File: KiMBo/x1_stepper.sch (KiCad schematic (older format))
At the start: 23 parts, among them U25 TMC2130

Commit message: More footprint association
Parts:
- R185, R186: footprint (none) -> Resistors_SMD:R_0805
- U25: footprint (none) -> KiMBo:QFN36_5X6
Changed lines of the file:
@@
 $EndComp
 $Comp
-L GND #PWR0250
+L GND #PWR0251
 U 1 1 5BA7E13F
 P 7500 3300
-F 0 "#PWR0250" H 7500 3050 50  0001 C CNN
+F 0 "#PWR0251" H 7500 3050 50  0001 C CNN
 F 1 "GND" H 7500 3150 50  0000 C CNN
 F 2 "" H 7500 3300 50  0000 C CNN
@@
 $EndComp
 $Comp
-L GND #PWR0251
+L GND #PWR0252
 U 1 1 58C092DF
 P 10350 3350
-F 0 "#PWR0251" H 10350 3100 50  0001 C CNN
+F 0 "#PWR0252" H 10350 3100 50  0001 C CNN
 F 1 "GND" H 10355 3177 50  0000 C CNN
 F 2 "" H 10350 3350 50  0000 C CNN
@@
 $EndComp
 $Comp
-L +24V #PWR0252
+L +24V #PWR0253
 U 1 1 5BA7E142
 P 8550 2850
-F 0 "#PWR0252" H 8550 2700 50  0001 C CNN
+F 0 "#PWR0253" H 8550 2700 50  0001 C CNN
 F 1 "+24V" H 8565 3023 50  0000 C CNN
 F 2 "" H 8550 2850 50  0000 C CNN
@@
 F 0 "R186" H 10700 6650 50  0000 R CNN
 F 1 "220mΩ" H 10700 6750 50  0000 R CNN
-F 2 "" V 10680 6700 50  0001 C CNN
+F 2 "Resistors_SMD:R_0805" V 10680 6700 50  0001 C CNN
 F 3 "" H 10750 6700 50  0000 C CNN
 	1    10750 6700
@@
 F 0 "R185" H 9900 6650 50  0000 R CNN
 F 1 "220mΩ" H 9900 6750 50  0000 R CNN
-F 2 "" V 9880 6700 50  0001 C CNN
+F 2 "Resistors_SMD:R_0805" V 9880 6700 50  0001 C CNN
 F 3 "" H 9950 6700 50  0000 C CNN
 	1    9950 6700
@@
 $EndComp
 $Comp
-L GND #PWR0253
+L GND #PWR0254
 U 1 1 58C09300
 P 9650 7050
-F 0 "#PWR0253" H 9650 6800 50  0001 C CNN
+F 0 "#PWR0254" H 9650 6800 50  0001 C CNN
 F 1 "GND" H 9655 6877 50  0000 C CNN
 F 2 "" H 9650 7050 50  0000 C CNN
@@
 NoConn ~ 7700 5700
 $Comp
-L GND #PWR0254
+L GND #PWR0255
 U 1 1 58C09323
 P 7650 6100
-F 0 "#PWR0254" H 7650 5850 50  0001 C CNN
+F 0 "#PWR0255" H 7650 5850 50  0001 C CNN
 F 1 "GND" H 7655 5927 50  0000 C CNN
 F 2 "" H 7650 6100 50  0000 C CNN
@@
 $EndComp
 $Comp
-L GND #PWR0255
+L GND #PWR0256
 U 1 1 5BA7E152
 P 9250 5200
-F 0 "#PWR0255" H 9250 4950 50  0001 C CNN
+F 0 "#PWR0256" H 9250 4950 50  0001 C CNN
 F 1 "GND" H 9250 5050 50  0000 C CNN
 F 2 "" H 9250 5200 50  0000 C CNN
@@
 $EndComp
 $Comp
-L GND #PWR0256
+L GND #PWR0257
 U 1 1 5BA7E155
 P 9250 6050
-F 0 "#PWR0256" H 9250 5800 50  0001 C CNN
+F 0 "#PWR0257" H 9250 5800 50  0001 C CNN
 F 1 "GND" H 9250 5900 50  0000 C CNN
 F 2 "" H 9250 6050 50  0000 C CNN
@@
 F 0 "U25" H 7950 6200 60  0000 C CNN
 F 1 "TMC2130" H 8700 6200 60  0000 C CNN
-F 2 "" H 8400 5000 60  0001 C CNN
+F 2 "KiMBo:QFN36_5X6" H 8400 5000 60  0001 C CNN
 F 3 "" H 8400 5000 60  0000 C CNN
 	1    8400 4700
@@
 	6400 3500 7700 3500
 $Comp
-L VDD_3V3B #PWR0257
+L VDD_3V3B #PWR0258
 U 1 1 5BA7E15A
 P 6750 3450
-F 0 "#PWR0257" H 6750 3300 50  0001 C CNN
+F 0 "#PWR0258" H 6750 3300 50  0001 C CNN
 F 1 "VDD_3V3B" H 6765 3623 50  0000 C CNN
 F 2 "" H 6750 3450 50  0000 C CNN

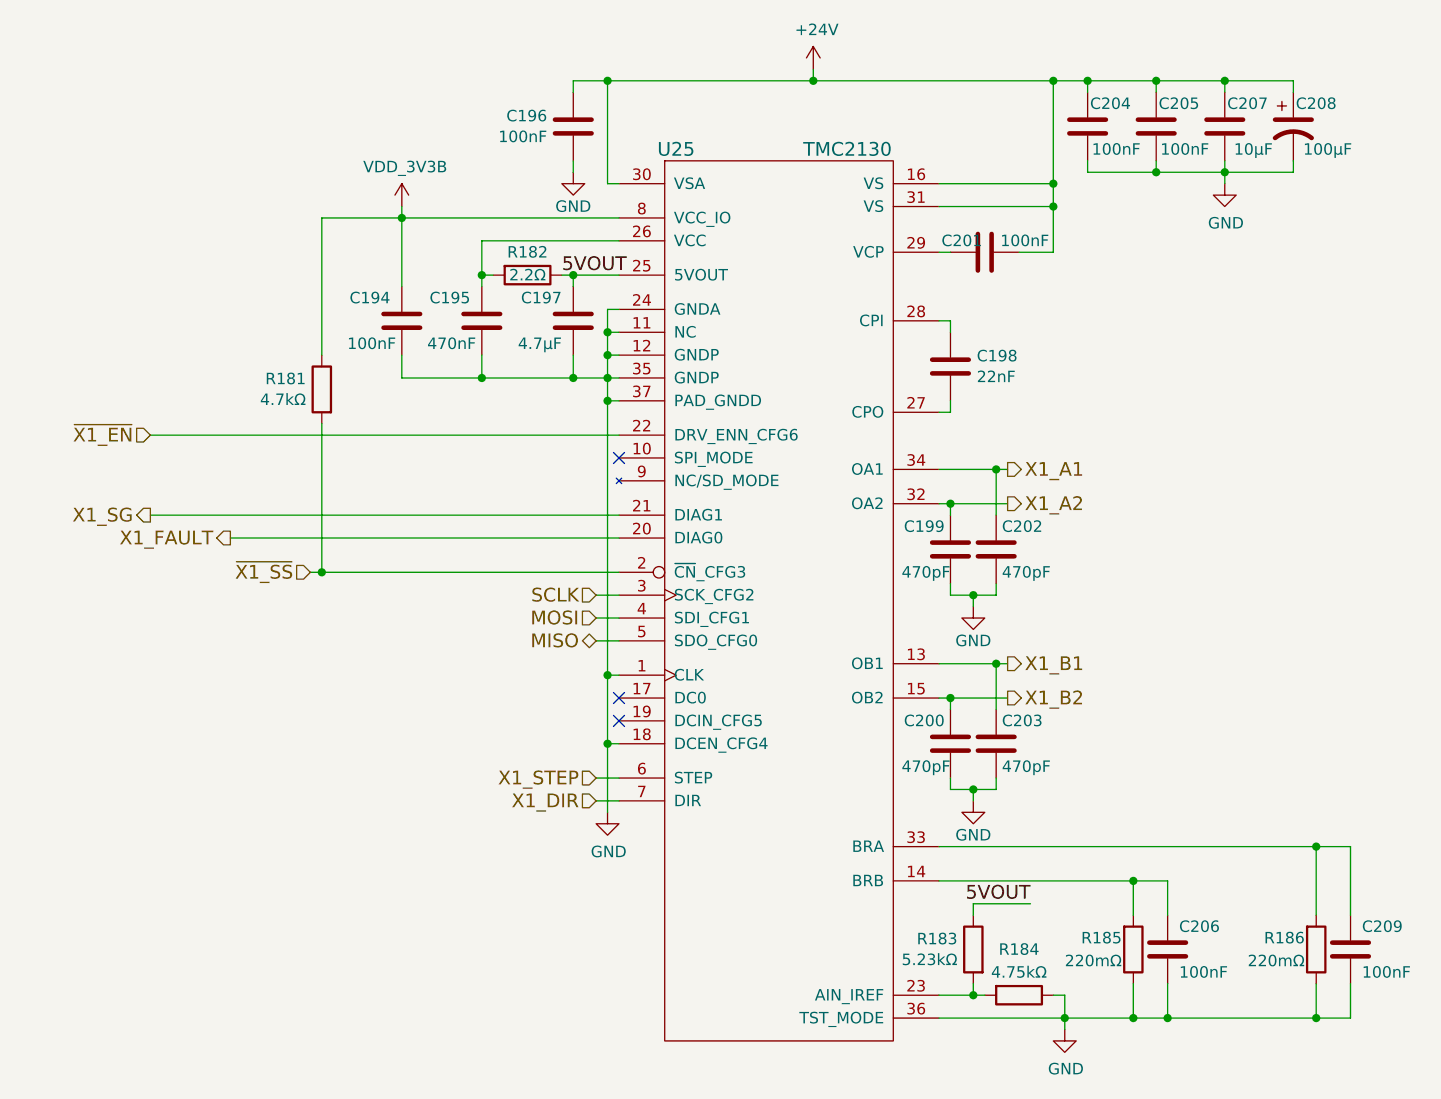
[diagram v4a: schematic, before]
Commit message: Add more footprints and more associations, one association left!
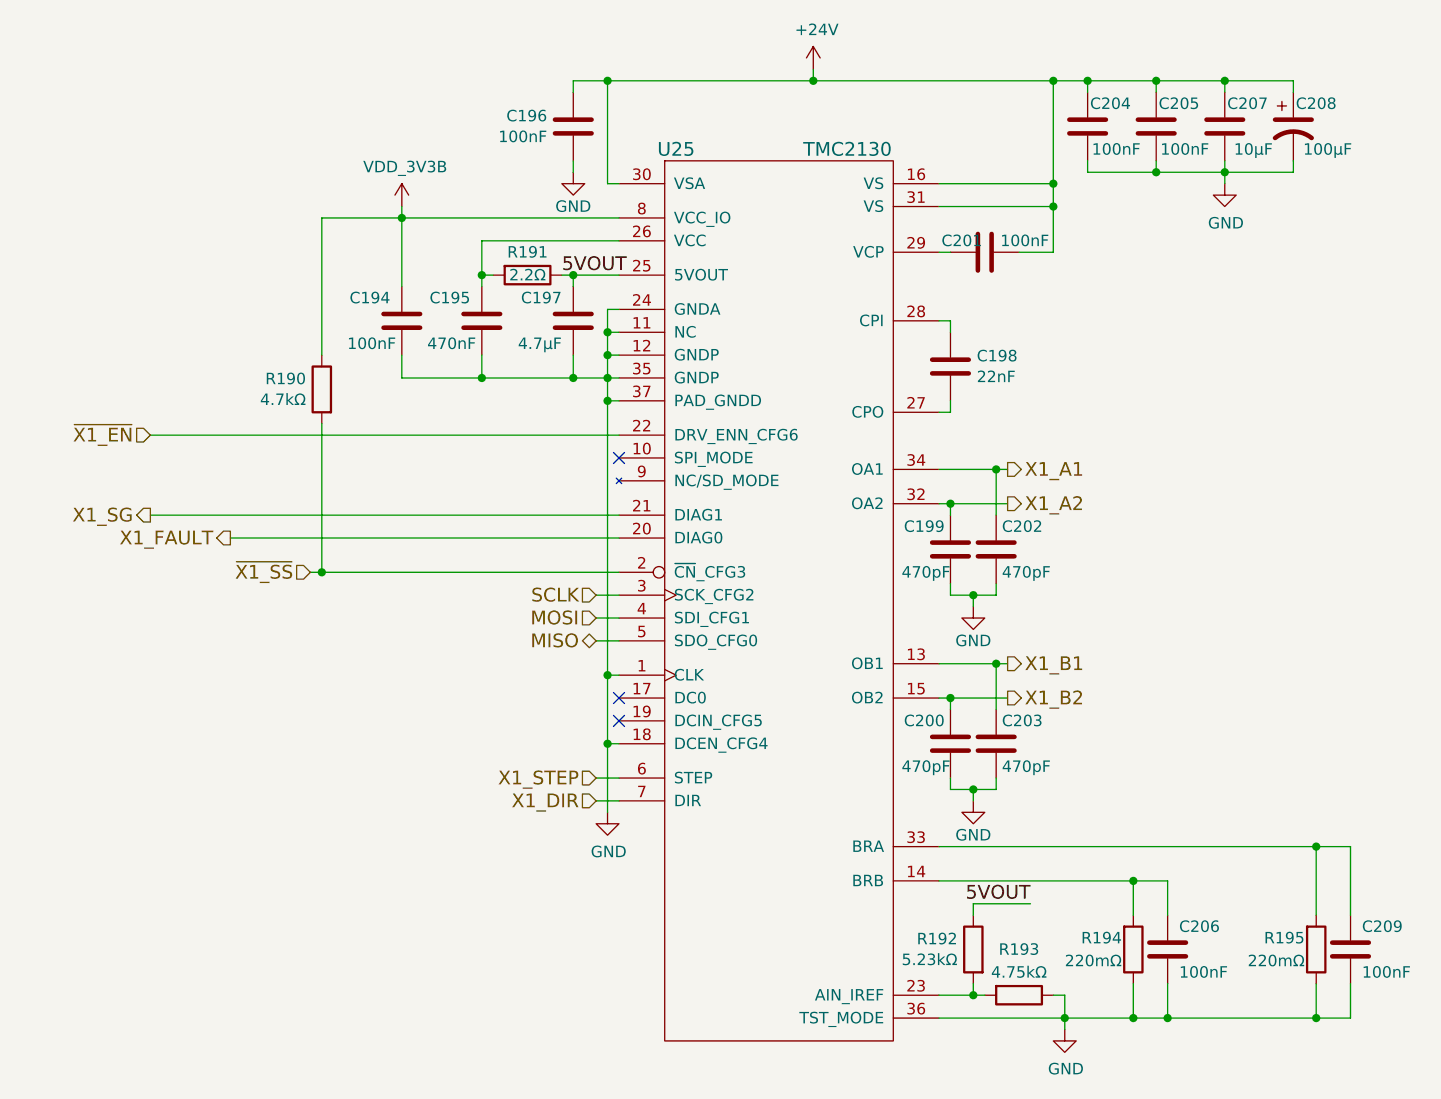
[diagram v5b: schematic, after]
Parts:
- R193: renamed from R184; footprint Resistors_SMD:R_0603 -> Resistors_SMD:R_0805
- R195: renamed from R186; footprint Resistors_SMD:R_0805 -> Resistors_SMD:R_0603
- renumbered R181 to R190, R182 to R191, R183 to R192, R185 to R194
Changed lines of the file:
@@
 $EndComp
 $Comp
-L GND #PWR0251
+L GND #PWR0253
 U 1 1 5BA7E13F
 P 7500 3300
-F 0 "#PWR0251" H 7500 3050 50  0001 C CNN
+F 0 "#PWR0253" H 7500 3050 50  0001 C CNN
 F 1 "GND" H 7500 3150 50  0000 C CNN
 F 2 "" H 7500 3300 50  0000 C CNN
@@
 $EndComp
 $Comp
-L GND #PWR0252
+L GND #PWR0254
 U 1 1 58C092DF
 P 10350 3350
-F 0 "#PWR0252" H 10350 3100 50  0001 C CNN
+F 0 "#PWR0254" H 10350 3100 50  0001 C CNN
 F 1 "GND" H 10355 3177 50  0000 C CNN
 F 2 "" H 10350 3350 50  0000 C CNN
@@
 $EndComp
 $Comp
-L +24V #PWR0253
+L +24V #PWR0255
 U 1 1 5BA7E142
 P 8550 2850
-F 0 "#PWR0253" H 8550 2700 50  0001 C CNN
+F 0 "#PWR0255" H 8550 2700 50  0001 C CNN
 F 1 "+24V" H 8565 3023 50  0000 C CNN
 F 2 "" H 8550 2850 50  0000 C CNN
@@
 $EndComp
 $Comp
-L R R186
+L R R195
 U 1 1 5BA7E144
 P 10750 6700
-F 0 "R186" H 10700 6650 50  0000 R CNN
+F 0 "R195" H 10700 6650 50  0000 R CNN
 F 1 "220mΩ" H 10700 6750 50  0000 R CNN
-F 2 "Resistors_SMD:R_0805" V 10680 6700 50  0001 C CNN
+F 2 "Resistors_SMD:R_0603" V 10680 6700 50  0001 C CNN
 F 3 "" H 10750 6700 50  0000 C CNN
 	1    10750 6700
@@
 $EndComp
 $Comp
-L R R185
+L R R194
 U 1 1 5BA7E145
 P 9950 6700
-F 0 "R185" H 9900 6650 50  0000 R CNN
+F 0 "R194" H 9900 6650 50  0000 R CNN
 F 1 "220mΩ" H 9900 6750 50  0000 R CNN
 F 2 "Resistors_SMD:R_0805" V 9880 6700 50  0001 C CNN
@@
 $EndComp
 $Comp
-L GND #PWR0254
+L GND #PWR0256
 U 1 1 58C09300
 P 9650 7050
-F 0 "#PWR0254" H 9650 6800 50  0001 C CNN
+F 0 "#PWR0256" H 9650 6800 50  0001 C CNN
 F 1 "GND" H 9655 6877 50  0000 C CNN
 F 2 "" H 9650 7050 50  0000 C CNN
@@
 NoConn ~ 7700 5600
 $Comp
-L R R182
+L R R191
 U 1 1 58C09307
 P 7300 3750
-F 0 "R182" V 7200 3750 50  0000 C CNN
+F 0 "R191" V 7200 3750 50  0000 C CNN
 F 1 "2.2Ω" V 7300 3750 50  0000 C CNN
 F 2 "Resistors_SMD:R_0603" V 7230 3750 50  0001 C CNN
@@
 NoConn ~ 7700 5700
 $Comp
-L GND #PWR0255
+L GND #PWR0257
 U 1 1 58C09323
 P 7650 6100
-F 0 "#PWR0255" H 7650 5850 50  0001 C CNN
+F 0 "#PWR0257" H 7650 5850 50  0001 C CNN
 F 1 "GND" H 7655 5927 50  0000 C CNN
 F 2 "" H 7650 6100 50  0000 C CNN
@@
 5VOUT
 $Comp
-L R R183
+L R R192
 U 1 1 58C09343
 P 9250 6700
-F 0 "R183" H 9319 6746 50  0000 L CNN
+F 0 "R192" H 9319 6746 50  0000 L CNN
 F 1 "5.23kΩ" H 9319 6655 50  0000 L CNN
 F 2 "Resistors_SMD:R_0603" V 9180 6700 50  0001 C CNN
@@
 5VOUT
 $Comp
-L R R184
+L R R193
 U 1 1 58C0934B
 P 9450 6900
-F 0 "R184" V 9250 6900 50  0000 C CNN
+F 0 "R193" V 9250 6900 50  0000 C CNN
 F 1 "4.75kΩ" V 9350 6900 50  0000 C CNN
-F 2 "Resistors_SMD:R_0603" V 9380 6900 50  0001 C CNN
+F 2 "Resistors_SMD:R_0805" V 9380 6900 50  0001 C CNN
 F 3 "" H 9450 6900 50  0000 C CNN
 	1    9450 6900
@@
 $EndComp
 $Comp
-L R R181
+L R R190
 U 1 1 5BA7E14F
 P 6400 4250
-F 0 "R181" H 6469 4296 50  0000 L CNN
+F 0 "R190" H 6469 4296 50  0000 L CNN
 F 1 "4.7kΩ" H 6469 4205 50  0000 L CNN
 F 2 "Resistors_SMD:R_0603" V 6330 4250 50  0001 C CNN
@@
 $EndComp
 $Comp
-L GND #PWR0256
+L GND #PWR0258
 U 1 1 5BA7E152
 P 9250 5200
-F 0 "#PWR0256" H 9250 4950 50  0001 C CNN
+F 0 "#PWR0258" H 9250 4950 50  0001 C CNN
 F 1 "GND" H 9250 5050 50  0000 C CNN
 F 2 "" H 9250 5200 50  0000 C CNN
@@
 $EndComp
 $Comp
-L GND #PWR0257
+L GND #PWR0259
 U 1 1 5BA7E155
 P 9250 6050
-F 0 "#PWR0257" H 9250 5800 50  0001 C CNN
+F 0 "#PWR0259" H 9250 5800 50  0001 C CNN
 F 1 "GND" H 9250 5900 50  0000 C CNN
 F 2 "" H 9250 6050 50  0000 C CNN
@@
 	6400 3500 7700 3500
 $Comp
-L VDD_3V3B #PWR0258
+L VDD_3V3B #PWR0260
 U 1 1 5BA7E15A
 P 6750 3450
-F 0 "#PWR0258" H 6750 3300 50  0001 C CNN
+F 0 "#PWR0260" H 6750 3300 50  0001 C CNN
 F 1 "VDD_3V3B" H 6765 3623 50  0000 C CNN
 F 2 "" H 6750 3450 50  0000 C CNN

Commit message: Begin layout
Arrange all connectors to get a feel for the area.
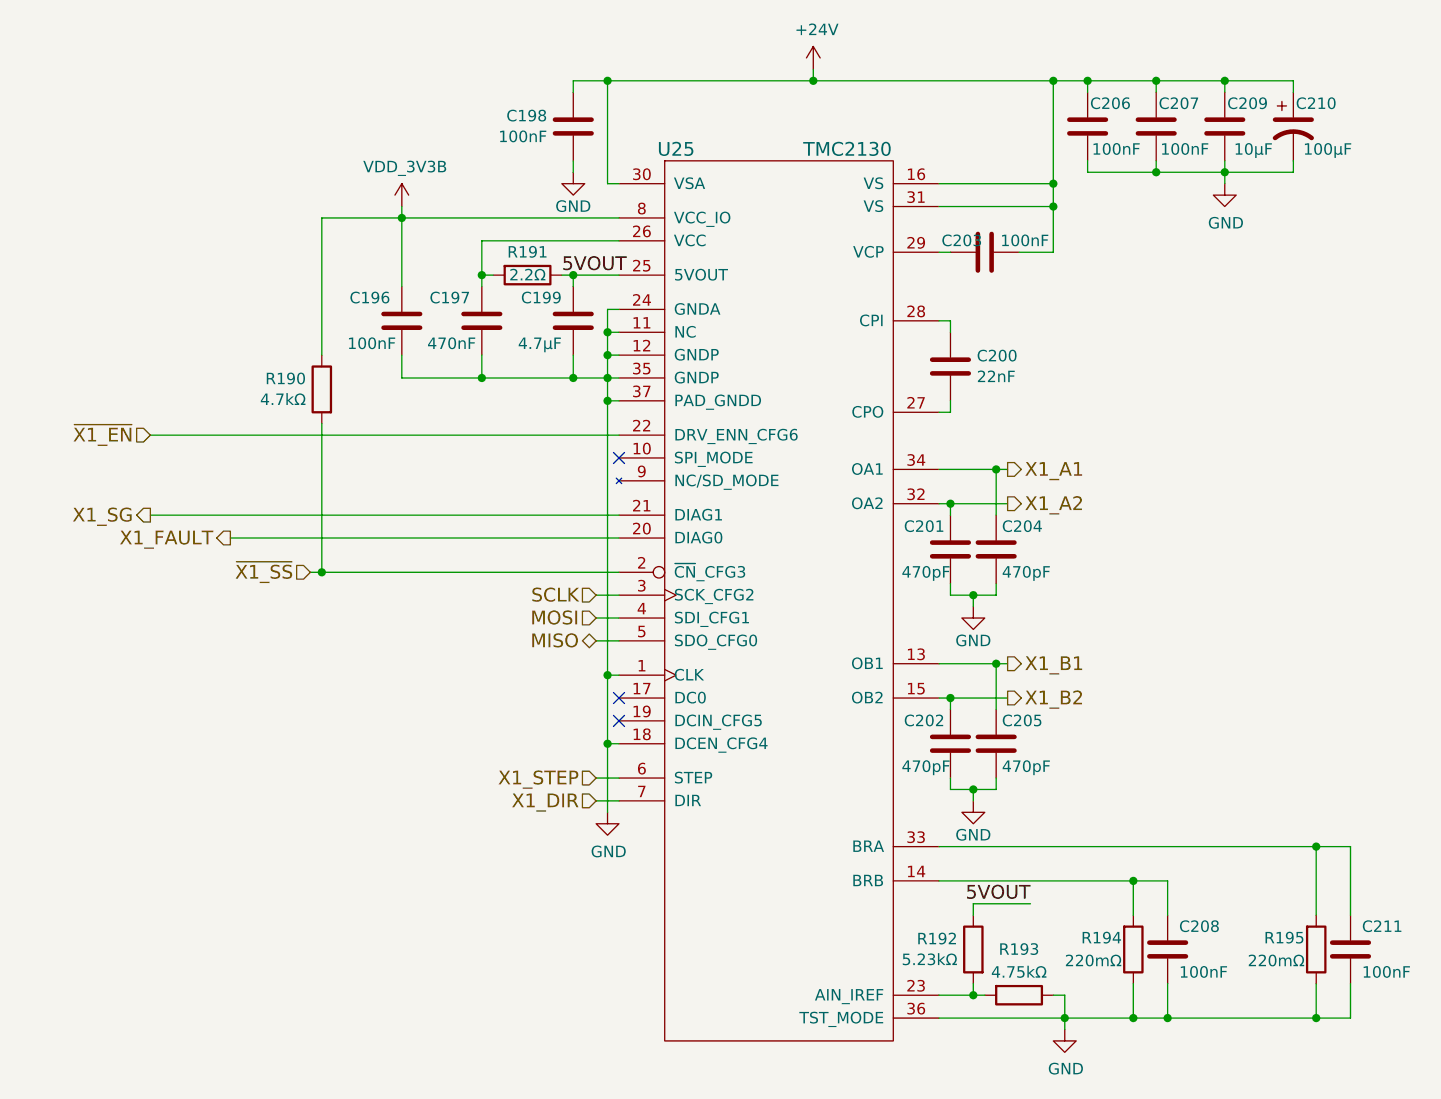
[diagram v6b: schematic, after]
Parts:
- renumbered C194 to C196, C195 to C197, C196 to C198, C197 to C199, C198 to C200, C199 to C201, C200 to C202, C201 to C203, C202 to C204, C203 to C205, C204 to C206, C205 to C207, C206 to C208, C207 to C209, C208 to C210, C209 to C211
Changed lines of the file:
@@
 X1_SG
 $Comp
-L C C196
+L C C198
 U 1 1 58C092B6
 P 7500 3100
-F 0 "C196" H 7386 3054 50  0000 R CNN
+F 0 "C198" H 7386 3054 50  0000 R CNN
 F 1 "100nF" H 7386 3145 50  0000 R CNN
 F 2 "Capacitors_SMD:C_0603" H 7538 2950 50  0001 C CNN
@@
 $EndComp
 $Comp
-L C C201
+L C C203
 U 1 1 58C092BD
 P 9300 3650
-F 0 "C201" V 9250 3550 50  0000 C CNN
+F 0 "C203" V 9250 3550 50  0000 C CNN
 F 1 "100nF" V 9250 3825 50  0000 C CNN
 F 2 "Capacitors_SMD:C_0603" H 9338 3500 50  0001 C CNN
@@
 $EndComp
 $Comp
-L CP1 C208
+L CP1 C210
 U 1 1 5BA7E13D
 P 10650 3100
-F 0 "C208" H 10750 3200 50  0000 C CNN
+F 0 "C210" H 10750 3200 50  0000 C CNN
 F 1 "100μF" H 10800 3000 50  0000 C CNN
 F 2 "Capacitors_SMD:c_elec_8x10" H 10650 3100 50  0001 C CNN
@@
 $EndComp
 $Comp
-L C C204
+L C C206
 U 1 1 5BA7E13E
 P 9750 3100
-F 0 "C204" H 9650 3200 50  0000 C CNN
+F 0 "C206" H 9650 3200 50  0000 C CNN
 F 1 "100nF" H 9625 3000 50  0000 C CNN
 F 2 "Capacitors_SMD:C_0603" H 9788 2950 50  0001 C CNN
@@
 $EndComp
 $Comp
-L GND #PWR0253
+L GND #PWR0256
 U 1 1 5BA7E13F
 P 7500 3300
-F 0 "#PWR0253" H 7500 3050 50  0001 C CNN
+F 0 "#PWR0256" H 7500 3050 50  0001 C CNN
 F 1 "GND" H 7500 3150 50  0000 C CNN
 F 2 "" H 7500 3300 50  0000 C CNN
@@
 $EndComp
 $Comp
-L C C205
+L C C207
 U 1 1 58C092D8
 P 10050 3100
-F 0 "C205" H 9950 3200 50  0000 C CNN
+F 0 "C207" H 9950 3200 50  0000 C CNN
 F 1 "100nF" H 9925 3000 50  0000 C CNN
 F 2 "Capacitors_SMD:C_0603" H 10088 2950 50  0001 C CNN
@@
 $EndComp
 $Comp
-L GND #PWR0254
+L GND #PWR0257
 U 1 1 58C092DF
 P 10350 3350
-F 0 "#PWR0254" H 10350 3100 50  0001 C CNN
+F 0 "#PWR0257" H 10350 3100 50  0001 C CNN
 F 1 "GND" H 10355 3177 50  0000 C CNN
 F 2 "" H 10350 3350 50  0000 C CNN
@@
 $EndComp
 $Comp
-L +24V #PWR0255
+L +24V #PWR0258
 U 1 1 5BA7E142
 P 8550 2850
-F 0 "#PWR0255" H 8550 2700 50  0001 C CNN
+F 0 "#PWR0258" H 8550 2700 50  0001 C CNN
 F 1 "+24V" H 8565 3023 50  0000 C CNN
 F 2 "" H 8550 2850 50  0000 C CNN
@@
 $EndComp
 $Comp
-L C C198
+L C C200
 U 1 1 5BA7E143
 P 9150 4150
-F 0 "C198" H 9265 4196 50  0000 L CNN
+F 0 "C200" H 9265 4196 50  0000 L CNN
 F 1 "22nF" H 9265 4105 50  0000 L CNN
 F 2 "Capacitors_SMD:C_0603" H 9188 4000 50  0001 C CNN
@@
 $EndComp
 $Comp
-L GND #PWR0256
+L GND #PWR0259
 U 1 1 58C09300
 P 9650 7050
-F 0 "#PWR0256" H 9650 6800 50  0001 C CNN
+F 0 "#PWR0259" H 9650 6800 50  0001 C CNN
 F 1 "GND" H 9655 6877 50  0000 C CNN
 F 2 "" H 9650 7050 50  0000 C CNN
@@
 $EndComp
 $Comp
-L C C195
+L C C197
 U 1 1 58C0930E
 P 7100 3950
-F 0 "C195" H 7150 4050 50  0000 L CNN
+F 0 "C197" H 7150 4050 50  0000 L CNN
 F 1 "470nF" H 7125 3850 50  0000 L CNN
 F 2 "Capacitors_SMD:C_0603" H 7138 3800 50  0001 C CNN
@@
 NoConn ~ 7700 5700
 $Comp
-L GND #PWR0257
+L GND #PWR0260
 U 1 1 58C09323
 P 7650 6100
-F 0 "#PWR0257" H 7650 5850 50  0001 C CNN
+F 0 "#PWR0260" H 7650 5850 50  0001 C CNN
 F 1 "GND" H 7655 5927 50  0000 C CNN
 F 2 "" H 7650 6100 50  0000 C CNN
@@
 $EndComp
 $Comp
-L C C206
+L C C208
 U 1 1 58C09329
 P 10100 6700
-F 0 "C206" H 10150 6800 50  0000 L CNN
+F 0 "C208" H 10150 6800 50  0000 L CNN
 F 1 "100nF" H 10150 6600 50  0000 L CNN
 F 2 "Capacitors_SMD:C_0603" H 10138 6550 50  0001 C CNN
@@
 NoConn ~ 7700 4550
 $Comp
-L C C197
+L C C199
 U 1 1 58C0933B
 P 7500 3950
-F 0 "C197" H 7550 4050 50  0000 L CNN
+F 0 "C199" H 7550 4050 50  0000 L CNN
 F 1 "4.7μF" H 7550 3850 50  0000 L CNN
 F 2 "Capacitors_SMD:C_0603" H 7538 3800 50  0001 C CNN
@@
 $EndComp
 $Comp
-L C C209
+L C C211
 U 1 1 5BA7E150
 P 10900 6700
-F 0 "C209" H 10950 6800 50  0000 L CNN
+F 0 "C211" H 10950 6800 50  0000 L CNN
 F 1 "100nF" H 10950 6600 50  0000 L CNN
 F 2 "Capacitors_SMD:C_0603" H 10938 6550 50  0001 C CNN
@@
 $EndComp
 $Comp
-L C C199
+L C C201
 U 1 1 5BA7E151
 P 9150 4950
-F 0 "C199" H 9175 5050 50  0000 L CNN
+F 0 "C201" H 9175 5050 50  0000 L CNN
 F 1 "470pF" H 9150 4850 50  0000 L CNN
 F 2 "Capacitors_SMD:C_0603" H 9188 4800 50  0001 C CNN
@@
 $EndComp
 $Comp
-L GND #PWR0258
+L GND #PWR0261
 U 1 1 5BA7E152
 P 9250 5200
-F 0 "#PWR0258" H 9250 4950 50  0001 C CNN
+F 0 "#PWR0261" H 9250 4950 50  0001 C CNN
 F 1 "GND" H 9250 5050 50  0000 C CNN
 F 2 "" H 9250 5200 50  0000 C CNN
@@
 $EndComp
 $Comp
-L C C202
+L C C204
 U 1 1 5BA7E153
 P 9350 4950
-F 0 "C202" H 9375 5050 50  0000 L CNN
+F 0 "C204" H 9375 5050 50  0000 L CNN
 F 1 "470pF" H 9375 4850 50  0000 L CNN
 F 2 "Capacitors_SMD:C_0603" H 9388 4800 50  0001 C CNN
@@
 $EndComp
 $Comp
-L C C200
+L C C202
 U 1 1 58C09377
 P 9150 5800
-F 0 "C200" H 9175 5900 50  0000 L CNN
+F 0 "C202" H 9175 5900 50  0000 L CNN
 F 1 "470pF" H 9150 5700 50  0000 L CNN
 F 2 "Capacitors_SMD:C_0603" H 9188 5650 50  0001 C CNN
@@
 $EndComp
 $Comp
-L GND #PWR0259
+L GND #PWR0262
 U 1 1 5BA7E155
 P 9250 6050
-F 0 "#PWR0259" H 9250 5800 50  0001 C CNN
+F 0 "#PWR0262" H 9250 5800 50  0001 C CNN
 F 1 "GND" H 9250 5900 50  0000 C CNN
 F 2 "" H 9250 6050 50  0000 C CNN
@@
 $EndComp
 $Comp
-L C C203
+L C C205
 U 1 1 5BA7E156
 P 9350 5800
-F 0 "C203" H 9375 5900 50  0000 L CNN
+F 0 "C205" H 9375 5900 50  0000 L CNN
 F 1 "470pF" H 9375 5700 50  0000 L CNN
 F 2 "Capacitors_SMD:C_0603" H 9388 5650 50  0001 C CNN
@@
 	9150 6000 9150 5950
 $Comp
-L C C207
+L C C209
 U 1 1 58C0940A
 P 10350 3100
-F 0 "C207" H 10250 3200 50  0000 C CNN
+F 0 "C209" H 10250 3200 50  0000 C CNN
 F 1 "10μF" H 10225 3000 50  0000 C CNN
 F 2 "Capacitors_SMD:C_0805" H 10388 2950 50  0001 C CNN
@@
 	6400 3500 7700 3500
 $Comp
-L VDD_3V3B #PWR0260
+L VDD_3V3B #PWR0263
 U 1 1 5BA7E15A
 P 6750 3450
-F 0 "#PWR0260" H 6750 3300 50  0001 C CNN
+F 0 "#PWR0263" H 6750 3300 50  0001 C CNN
 F 1 "VDD_3V3B" H 6765 3623 50  0000 C CNN
 F 2 "" H 6750 3450 50  0000 C CNN
@@
 $EndComp
 $Comp
-L C C194
+L C C196
 U 1 1 5A89A0A1
 P 6750 3950
-F 0 "C194" H 6800 4050 50  0000 L CNN
+F 0 "C196" H 6800 4050 50  0000 L CNN
 F 1 "100nF" H 6775 3850 50  0000 L CNN
 F 2 "Capacitors_SMD:C_0603" H 6788 3800 50  0001 C CNN
